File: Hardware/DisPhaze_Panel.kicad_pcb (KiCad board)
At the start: 2 copper layers, 60.8 x 128.5 mm, 15 parts

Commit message: Panel First Draft
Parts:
- added G***: LOGO, logo:disphaze, B.Cu at (129.6, 45.8)
- added Ref**: Oval_Mounting_Hole, Custom_Footprints:Oval_Mounting_Hole, F.Cu at (107.1, 166.3)
- added Ref**: Oval_Mounting_Hole, Custom_Footprints:Oval_Mounting_Hole, F.Cu at (152.9, 43.8)
- added Ref**: Oval_Mounting_Hole, Custom_Footprints:Oval_Mounting_Hole, F.Cu at (152.9, 166.3)
- added Ref**: Oval_Mounting_Hole, Custom_Footprints:Oval_Mounting_Hole, F.Cu at (107.1, 43.8)
- moved Ref** 0.06 mm to (147.5, 109.5)
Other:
- board text added: "+1"
- board text added: "+2"
- board text added: "-1"
- board text added: "-2"
- board text added: "0"
- board text added: "1"
- board text added: "1V/O"
- board text added: "2"
- board text added: "Amount"
- board text added: "CV1"
- board text added: "CV2"
- board text added: "Fine Tune"
- board text added: "Mountjoy Modular"
- board text added: "Oct"
- board text added: "Octave"
- board text added: "Out 1"
- board text added: "Out 2"
- board text added: "VCA"
- board text removed: "DAC1 Out"
- board text removed: "DAC2 Out"
- board text removed: "PD1 Amt"
- board text removed: "PD2 Amt"
- board text removed: "Pitch In"
- board text removed: "VCA In"

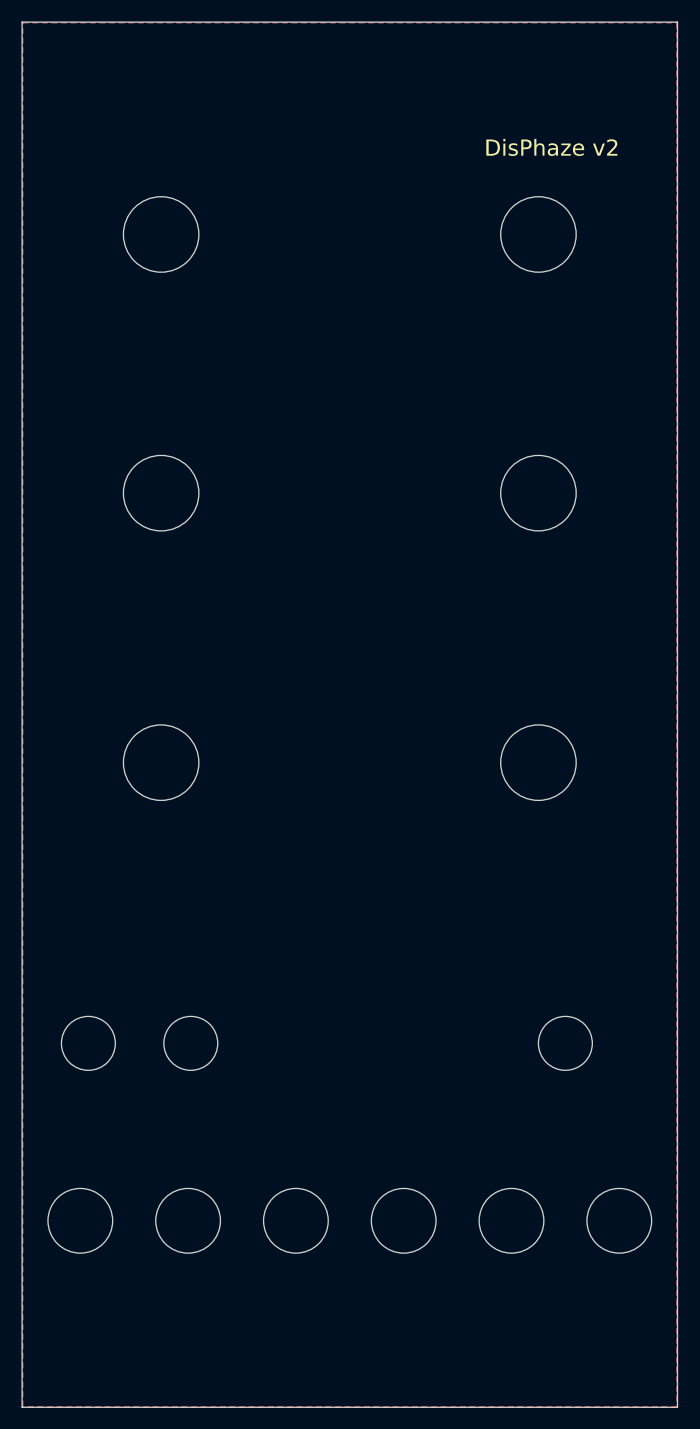
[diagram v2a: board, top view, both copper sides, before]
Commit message: Calibration settings can be saved to Flash memory and finalised PCB and panel for manufacture
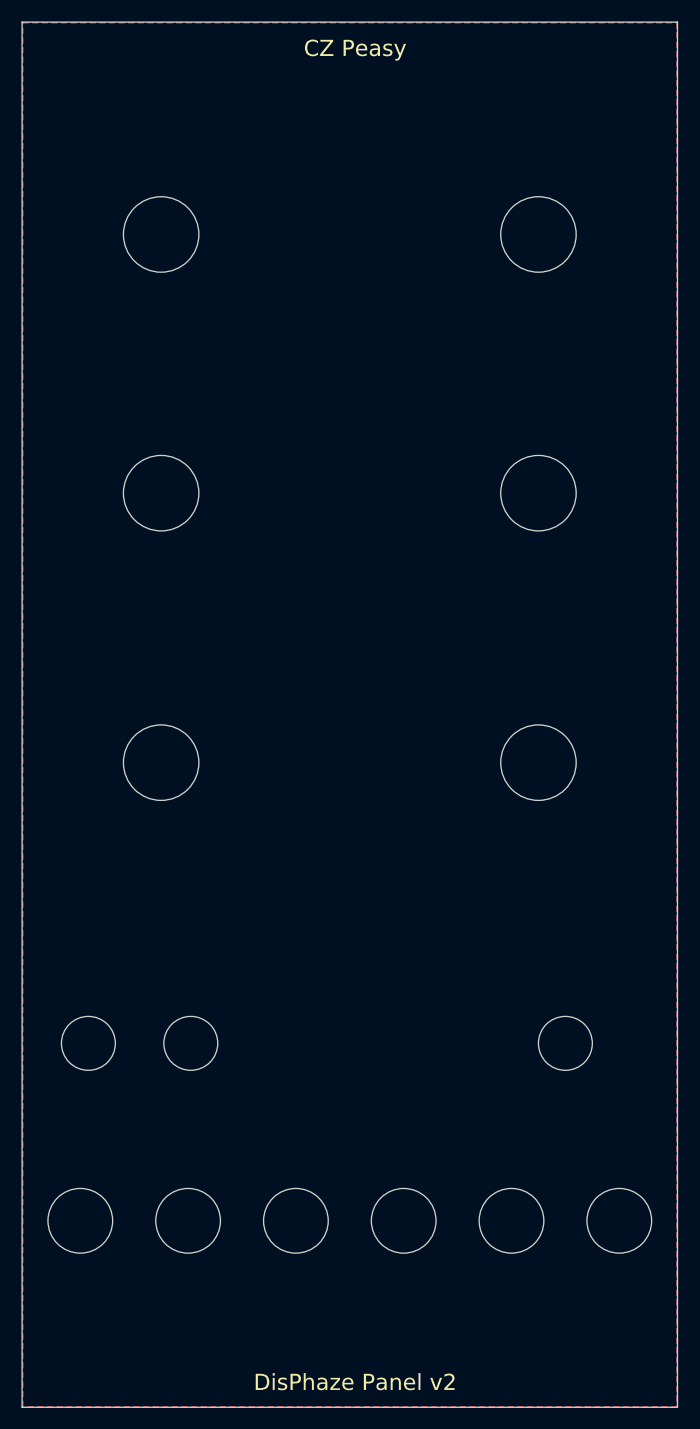
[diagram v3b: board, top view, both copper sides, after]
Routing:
- added copper zone on B.Cu, net (none)
- added copper zone on F.Cu, net (none)
- removed copper zone on B.Cu, net GND
- removed copper zone on F.Cu, net GND
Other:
- board text added: "CZ Peasy"
- board text added: "DisPhaze Panel v2"
- board text removed: "DisPhaze v2"
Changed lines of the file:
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@@
   (general
     (thickness 1.6)
-    (drawings 99)
+    (drawings 100)
     (tracks 0)
     (zones 0)
     (modules 20)
-    (nets 2)
+    (nets 1)
   )
   (page A4)
@@
     (35 F.Paste user)
     (36 B.SilkS user)
-    (37 F.SilkS user hide)
+    (37 F.SilkS user)
     (38 B.Mask user)
     (39 F.Mask user)
@@
       (psnegative false)
       (psa4output false)
-      (plotreference true)
-      (plotvalue true)
+      (plotreference false)
+      (plotvalue false)
       (plotinvisibletext false)
       (padsonsilk false)
@@
       (outputformat 1)
       (mirror false)
-      (drillshape 1)
+      (drillshape 0)
       (scaleselection 1)
-      (outputdirectory ""))
+      (outputdirectory "Gerbers/Panel/"))
   )
   (net 0 "")
-  (net 1 GND)
   (net_class Default "This is the default net class."
     (clearance 0.2)
@@
     (uvia_dia 0.3)
     (uvia_drill 0.1)
+  )
+  (module Custom_Footprints:Oval_Mounting_Hole (layer F.Cu)
+    (at 152.9 43.8)
+    (descr "Mounting Hole 6mm, no annular")
+    (tags "mounting hole 6mm no annular")
+    (fp_text reference Ref** (at 0 -3.5) (layer F.SilkS) hide
+      (effects (font (size 1 1) (thickness 0.15)))
+    )
+    (fp_text value Oval_Mounting_Hole (at 0 5.08) (layer F.Fab)
+      (effects (font (size 1 1) (thickness 0.15)))
+    )
+    (fp_line (start 5.08 -3) (end 7.5 -3) (layer Dwgs.User) (width 0.15))
+    (fp_line (start 5.08 3) (end 7.5 3) (layer Dwgs.User) (width 0.15))
+    (fp_line (start 7.5 1.27) (end 7.5 3) (layer Dwgs.User) (width 0.15))
+    (fp_line (start 7.5 -3) (end 7.5 -1.27) (layer Dwgs.User) (width 0.15))
+    (fp_line (start -7.5 3) (end -5.08 3) (layer Dwgs.User) (width 0.15))
+    (fp_line (start -7.5 -3) (end -5.08 -3) (layer Dwgs.User) (width 0.15))
+    (fp_line (start -7.5 1.27) (end -7.5 3) (layer Dwgs.User) (width 0.15))
+    (fp_line (start -7.5 -3) (end -7.5 -1.27) (layer Dwgs.User) (width 0.15))
+    (fp_circle (center 0 0) (end 1.54 0) (layer Cmts.User) (width 0.15))
+    (pad "" np_thru_hole oval (at 0 0) (size 5 3.2) (drill oval 5 3.2) (layers *.Cu *.Mask))
   )
   (module Custom_Footprints:Oval_Mounting_Hole (layer F.Cu)
@@
     (fp_circle (center 0 0) (end 4.5 0) (layer F.CrtYd) (width 0.05))
     (pad "" np_thru_hole circle (at 0 0) (size 6 6) (drill 6) (layers *.Cu *.Mask))
-  )
-  (module Custom_Footprints:Oval_Mounting_Hole (layer F.Cu)
-    (at 152.9 43.8)
-    (descr "Mounting Hole 6mm, no annular")
-    (tags "mounting hole 6mm no annular")
-    (fp_text reference Ref** (at 0 -3.5) (layer F.SilkS) hide
-      (effects (font (size 1 1) (thickness 0.15)))
-    )
-    (fp_text value Oval_Mounting_Hole (at 0 5.08) (layer F.Fab)
-      (effects (font (size 1 1) (thickness 0.15)))
-    )
-    (fp_line (start 5.08 -3) (end 7.5 -3) (layer Dwgs.User) (width 0.15))
-    (fp_line (start 5.08 3) (end 7.5 3) (layer Dwgs.User) (width 0.15))
-    (fp_line (start 7.5 1.27) (end 7.5 3) (layer Dwgs.User) (width 0.15))
-    (fp_line (start 7.5 -3) (end 7.5 -1.27) (layer Dwgs.User) (width 0.15))
-    (fp_line (start -7.5 3) (end -5.08 3) (layer Dwgs.User) (width 0.15))
-    (fp_line (start -7.5 -3) (end -5.08 -3) (layer Dwgs.User) (width 0.15))
-    (fp_line (start -7.5 1.27) (end -7.5 3) (layer Dwgs.User) (width 0.15))
-    (fp_line (start -7.5 -3) (end -7.5 -1.27) (layer Dwgs.User) (width 0.15))
-    (fp_circle (center 0 0) (end 1.54 0) (layer Cmts.User) (width 0.15))
-    (pad "" np_thru_hole oval (at 0 0) (size 5 3.2) (drill oval 5 3.2) (layers *.Cu *.Mask))
   )
   (module logo:disphaze (layer B.Cu)
@@
       (xy -13.763019 2.246289) (xy -12.971529 2.273395) (xy -12.286705 2.174484)) (layer B.Mask) (width 0.01))
   )
+  (gr_text "CZ Peasy" (at 130.5 43.25) (layer F.SilkS)
+    (effects (font (size 1.5 1.5) (thickness 0.3)))
+  )
   (gr_line (start 112.5 101) (end 112.5 102.25) (layer B.Mask) (width 0.4))
   (gr_line (start 139 60.5) (end 136.5 60.5) (layer B.Mask) (width 1))
@@
   (gr_line (start 122.75 84.5) (end 117.5 84.5) (layer B.Mask) (width 1))
   (gr_line (start 142.5 84.5) (end 137.25 84.5) (layer B.Mask) (width 1))
-  (gr_text 2 (at 105 73.75) (layer B.Mask)
+  (gr_text 2 (at 105 74) (layer B.Mask)
     (effects (font (size 4 4) (thickness 1)) (justify mirror))
   )
@@
   (gr_line (start 133 70.5) (end 130 70.5) (layer B.Mask) (width 0.4))
   (gr_line (start 133 73.52) (end 133 70.5) (layer B.Mask) (width 0.4))
-  (gr_text CV1 (at 145.2 159.4) (layer B.Mask)
-    (effects (font (size 2 2) (thickness 0.3)) (justify mirror))
-  )
-  (gr_text "Mountjoy Modular" (at 130.5 166.75) (layer B.Mask)
+  (gr_text CV1 (at 145.2 159.5) (layer B.Mask)
+    (effects (font (size 2 2) (thickness 0.3)) (justify mirror))
+  )
+  (gr_text "Mountjoy Modular" (at 130 166.75) (layer B.Mask)
     (effects (font (size 2 2) (thickness 0.2)) (justify mirror))
   )
@@
     (effects (font (size 2 2) (thickness 0.3)) (justify mirror))
   )
-  (gr_text VCA (at 124.5 159.6) (layer B.Mask)
+  (gr_text VCA (at 124.5 159.5) (layer B.Mask)
     (effects (font (size 2 2) (thickness 0.3)) (justify mirror))
   )
@@
     (effects (font (size 2 2) (thickness 0.3)) (justify mirror))
   )
-  (gr_text "DisPhaze v2" (at 148.75 52.5) (layer F.SilkS)
+  (gr_text "DisPhaze Panel v2" (at 130.5 167) (layer F.SilkS)
     (effects (font (size 1.5 1.5) (thickness 0.3)))
   )
@@
   (gr_line (start 100 50) (end 100 160) (layer Dwgs.User) (width 0.2))
   (gr_line (start 100 50) (end 160 50) (layer Dwgs.User) (width 0.2))
-  (zone (net 1) (net_name GND) (layer B.Cu) (hatch edge 0.508)
+  (zone (net 0) (net_name "") (layer B.Cu) (hatch edge 0.508)
     (connect_pads (clearance 0.508))
     (min_thickness 0.254)
@@
     )
   )
-  (zone (net 1) (net_name GND) (layer F.Cu) (hatch edge 0.508)
+  (zone (net 0) (net_name "") (layer F.Cu) (hatch edge 0.508)
     (connect_pads (clearance 0.508))
     (min_thickness 0.254)

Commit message: New Panel sent for manufacture
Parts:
- Ref** (x6): footprint Custom_Footprints:Alpha_9mm_Pot_MountingHole_7mm -> Custom_Footprints:Alpha_9mm_pot_hole; moved to B.Cu
- Ref** (x9): moved to B.Cu
- moved G1 0.71 mm to (129.7, 45.1)
- renumbered G*** to G1
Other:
- board text added: "DisPhaze Panel v3"
- board text added: "JLCJLCJLCJLC"
- board text removed: "+1"
- board text removed: "+2"
- board text removed: "-1"
- board text removed: "-2"
- board text removed: "0"
- board text removed: "1"
- board text removed: "2"
- board text removed: "Amount"
- board text removed: "DisPhaze Panel v2"
